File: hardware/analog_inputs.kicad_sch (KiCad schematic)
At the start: 0 parts

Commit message: Add the Cube project
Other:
- sheet Analog Input 1 ports: added REF; removed none
- sheet Analog Input 2 ports: added REF; removed none
- sheet Analog Input 3 ports: added REF; removed none
- sheet Analog Input 4 ports: added REF; removed none
- title: (none) -> Analog Inputs
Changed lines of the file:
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@@
   (paper "A4")
   (title_block
-    (date "2023-06-06")
+    (title "Analog Inputs")
+    (date "2023-07-01")
     (rev "${REVISION}")
     (company "Author: I. Kajdan")
     (comment 1 "Reviewer:")
   )
-  (wire (pts (xy 133.35 107.95) (xy 134.62 107.95))
+  (wire (pts (xy 135.89 104.14) (xy 137.16 104.14))
     (stroke (width 0) (type default))
   )
-  (wire (pts (xy 162.56 96.52) (xy 163.83 96.52))
+  (wire (pts (xy 165.1 92.71) (xy 166.37 92.71))
     (stroke (width 0) (type default))
   )
-  (wire (pts (xy 133.35 85.09) (xy 134.62 85.09))
+  (wire (pts (xy 135.89 107.95) (xy 137.16 107.95))
     (stroke (width 0) (type default))
   )
-  (wire (pts (xy 162.56 119.38) (xy 163.83 119.38))
+  (wire (pts (xy 135.89 81.28) (xy 137.16 81.28))
     (stroke (width 0) (type default))
   )
-  (wire (pts (xy 133.35 119.38) (xy 134.62 119.38))
+  (wire (pts (xy 165.1 115.57) (xy 166.37 115.57))
     (stroke (width 0) (type default))
   )
-  (wire (pts (xy 162.56 85.09) (xy 163.83 85.09))
+  (wire (pts (xy 135.89 115.57) (xy 137.16 115.57))
     (stroke (width 0) (type default))
   )
-  (wire (pts (xy 162.56 107.95) (xy 163.83 107.95))
+  (wire (pts (xy 135.89 96.52) (xy 137.16 96.52))
     (stroke (width 0) (type default))
   )
-  (wire (pts (xy 133.35 96.52) (xy 134.62 96.52))
+  (wire (pts (xy 135.89 119.38) (xy 137.16 119.38))
     (stroke (width 0) (type default))
   )
-  (hierarchical_label "IN4" (shape input) (at 133.35 119.38 180) (fields_autoplaced)
+  (wire (pts (xy 165.1 81.28) (xy 166.37 81.28))
+    (stroke (width 0) (type default))
+  )
+  (wire (pts (xy 135.89 85.09) (xy 137.16 85.09))
+    (stroke (width 0) (type default))
+  )
+  (wire (pts (xy 165.1 104.14) (xy 166.37 104.14))
+    (stroke (width 0) (type default))
+  )
+  (wire (pts (xy 135.89 92.71) (xy 137.16 92.71))
+    (stroke (width 0) (type default))
+  )
+  (hierarchical_label "REF1" (shape input) (at 135.89 107.95 180) (fields_autoplaced)
     (effects (font (size 1.27 1.27)) (justify right))
   )
-  (hierarchical_label "OUT2" (shape output) (at 163.83 96.52 0) (fields_autoplaced)
+  (hierarchical_label "IN4" (shape input) (at 135.89 115.57 180) (fields_autoplaced)
+    (effects (font (size 1.27 1.27)) (justify right))
+  )
+  (hierarchical_label "OUT2" (shape output) (at 166.37 92.71 0) (fields_autoplaced)
     (effects (font (size 1.27 1.27)) (justify left))
   )
-  (hierarchical_label "OUT4" (shape output) (at 163.83 119.38 0) (fields_autoplaced)
+  (hierarchical_label "REF2" (shape input) (at 135.89 96.52 180) (fields_autoplaced)
+    (effects (font (size 1.27 1.27)) (justify right))
+  )
+  (hierarchical_label "OUT4" (shape output) (at 166.37 115.57 0) (fields_autoplaced)
     (effects (font (size 1.27 1.27)) (justify left))
   )
-  (hierarchical_label "IN3" (shape input) (at 133.35 107.95 180) (fields_autoplaced)
+  (hierarchical_label "REF2" (shape input) (at 135.89 119.38 180) (fields_autoplaced)
     (effects (font (size 1.27 1.27)) (justify right))
   )
-  (hierarchical_label "OUT3" (shape output) (at 163.83 107.95 0) (fields_autoplaced)
+  (hierarchical_label "REF1" (shape input) (at 135.89 85.09 180) (fields_autoplaced)
+    (effects (font (size 1.27 1.27)) (justify right))
+  )
+  (hierarchical_label "IN3" (shape input) (at 135.89 104.14 180) (fields_autoplaced)
+    (effects (font (size 1.27 1.27)) (justify right))
+  )
+  (hierarchical_label "OUT3" (shape output) (at 166.37 104.14 0) (fields_autoplaced)
     (effects (font (size 1.27 1.27)) (justify left))
   )
-  (hierarchical_label "IN1" (shape input) (at 133.35 85.09 180) (fields_autoplaced)
+  (hierarchical_label "IN1" (shape input) (at 135.89 81.28 180) (fields_autoplaced)
     (effects (font (size 1.27 1.27)) (justify right))
   )
-  (hierarchical_label "OUT1" (shape output) (at 163.83 85.09 0) (fields_autoplaced)
+  (hierarchical_label "OUT1" (shape output) (at 166.37 81.28 0) (fields_autoplaced)
     (effects (font (size 1.27 1.27)) (justify left))
   )
-  (hierarchical_label "IN2" (shape input) (at 133.35 96.52 180) (fields_autoplaced)
+  (hierarchical_label "IN2" (shape input) (at 135.89 92.71 180) (fields_autoplaced)
     (effects (font (size 1.27 1.27)) (justify right))
   )
-  (sheet (at 134.62 81.28) (size 27.94 7.62)
+  (sheet (at 137.16 78.74) (size 27.94 8.89)
     (stroke (width 0.1524) (type solid))
     (fill (color 0 0 0 0.0000))
-    (property "Sheetname" "Analog Input 1" (at 148.59 84.3784 0)
-      (effects (font (size 1.27 1.27)) (justify top))
+    (property "Sheetname" "Analog Input 1" (at 151.13 83.1084 0)
+      (effects (font (size 1.27 1.27)))
     )
-    (property "Sheetfile" "analog_input.kicad_sch" (at 134.62 98.3746 0)
+    (property "Sheetfile" "analog_input.kicad_sch" (at 137.16 95.8346 0)
       (effects (font (size 1.27 1.27)) (justify left top) hide)
     )
-    (pin "IN" input (at 134.62 85.09 180)
+    (pin "IN" input (at 137.16 81.28 180)
       (effects (font (size 1.27 1.27)) (justify left))
     )
-    (pin "OUT" output (at 162.56 85.09 0)
+    (pin "OUT" output (at 165.1 81.28 0)
       (effects (font (size 1.27 1.27)) (justify right))
+    )
+    (pin "REF" input (at 137.16 85.09 180)
+      (effects (font (size 1.27 1.27)) (justify left))
     )
     (instances
@@
     )
   )
-  (sheet (at 134.62 104.14) (size 27.94 7.62)
+  (sheet (at 137.16 101.6) (size 27.94 8.89)
     (stroke (width 0.1524) (type solid))
     (fill (color 0 0 0 0.0000))
-    (property "Sheetname" "Analog Input 3" (at 148.59 107.2384 0)
+    (property "Sheetname" "Analog Input 3" (at 151.13 104.6984 0)
       (effects (font (size 1.27 1.27)) (justify top))
     )
-    (property "Sheetfile" "analog_input.kicad_sch" (at 134.62 121.2346 0)
+    (property "Sheetfile" "analog_input.kicad_sch" (at 137.16 118.6946 0)
       (effects (font (size 1.27 1.27)) (justify left top) hide)
     )
-    (pin "IN" input (at 134.62 107.95 180)
+    (pin "IN" input (at 137.16 104.14 180)
       (effects (font (size 1.27 1.27)) (justify left))
     )
-    (pin "OUT" output (at 162.56 107.95 0)
+    (pin "OUT" output (at 165.1 104.14 0)
       (effects (font (size 1.27 1.27)) (justify right))
+    )
+    (pin "REF" input (at 137.16 107.95 180)
+      (effects (font (size 1.27 1.27)) (justify left))
     )
     (instances
@@
     )
   )
-  (sheet (at 134.62 115.57) (size 27.94 7.62)
+  (sheet (at 137.16 113.03) (size 27.94 8.89)
     (stroke (width 0.1524) (type solid))
     (fill (color 0 0 0 0.0000))
-    (property "Sheetname" "Analog Input 4" (at 148.59 118.6684 0)
+    (property "Sheetname" "Analog Input 4" (at 151.13 116.1284 0)
       (effects (font (size 1.27 1.27)) (justify top))
     )
-    (property "Sheetfile" "analog_input.kicad_sch" (at 134.62 132.6646 0)
+    (property "Sheetfile" "analog_input.kicad_sch" (at 137.16 130.1246 0)
       (effects (font (size 1.27 1.27)) (justify left top) hide)
     )
-    (pin "IN" input (at 134.62 119.38 180)
+    (pin "IN" input (at 137.16 115.57 180)
       (effects (font (size 1.27 1.27)) (justify left))
     )
-    (pin "OUT" output (at 162.56 119.38 0)
+    (pin "OUT" output (at 165.1 115.57 0)
       (effects (font (size 1.27 1.27)) (justify right))
+    )
+    (pin "REF" input (at 137.16 119.38 180)
+      (effects (font (size 1.27 1.27)) (justify left))
     )
     (instances
@@
     )
   )
-  (sheet (at 134.62 92.71) (size 27.94 7.62)
+  (sheet (at 137.16 90.17) (size 27.94 8.89)
     (stroke (width 0.1524) (type solid))
     (fill (color 0 0 0 0.0000))
-    (property "Sheetname" "Analog Input 2" (at 148.59 95.8084 0)
+    (property "Sheetname" "Analog Input 2" (at 151.13 93.2684 0)
       (effects (font (size 1.27 1.27)) (justify top))
     )
-    (property "Sheetfile" "analog_input.kicad_sch" (at 134.62 109.8046 0)
+    (property "Sheetfile" "analog_input.kicad_sch" (at 137.16 107.2646 0)
       (effects (font (size 1.27 1.27)) (justify left top) hide)
     )
-    (pin "IN" input (at 134.62 96.52 180)
+    (pin "IN" input (at 137.16 92.71 180)
       (effects (font (size 1.27 1.27)) (justify left))
     )
-    (pin "OUT" output (at 162.56 96.52 0)
+    (pin "OUT" output (at 165.1 92.71 0)
       (effects (font (size 1.27 1.27)) (justify right))
     )
+    (pin "REF" input (at 137.16 96.52 180)
+      (effects (font (size 1.27 1.27)) (justify left))
+    )
     (instances

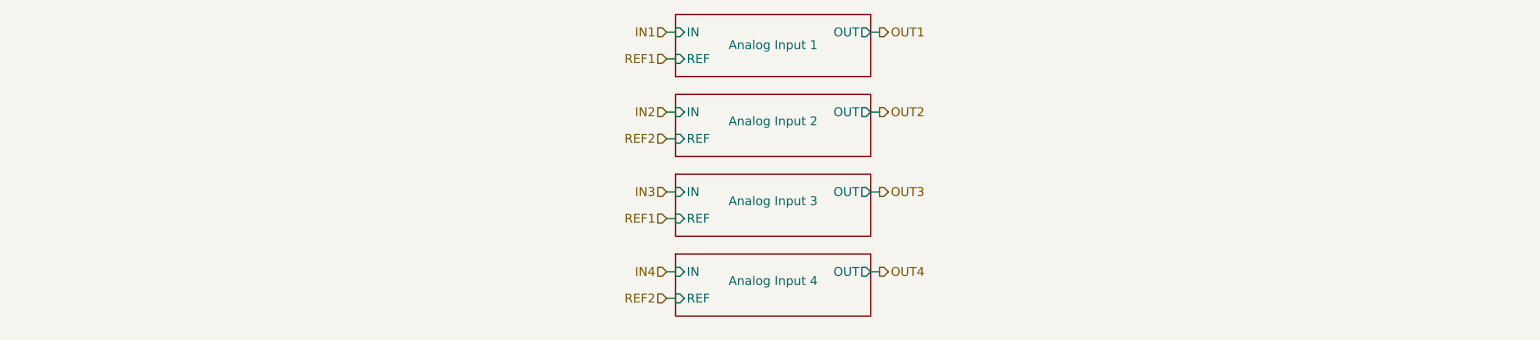
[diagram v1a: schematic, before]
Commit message: Improve the schematic
- add anti-aliasing filters
- rearrange the main connector signals
- improve the power filtering
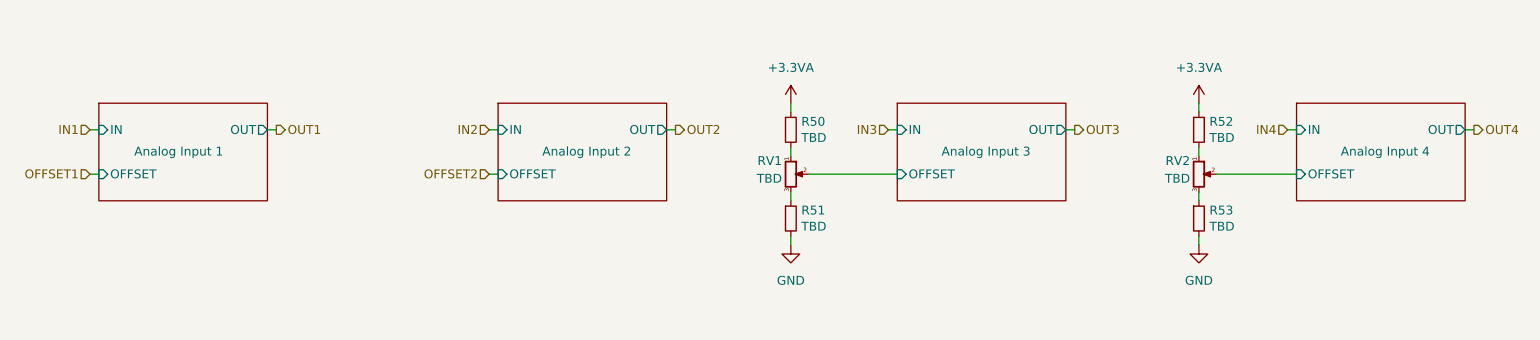
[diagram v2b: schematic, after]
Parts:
- added R50, R51, R52, R53: TBD, Resistor_SMD:R_0603_1608Metric_Pad0.98x0.95mm_HandSolder, symbol Device:R_Small
- added RV1, RV2: TBD, Potentiometer_SMD:Potentiometer_Bourns_3214J_Horizontal, symbol Device:R_Potentiometer_Small
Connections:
- new net: R51.1, RV1.3
- new net: R52.2, RV2.1
- new net: R50.2, RV1.1
- new net: R53.1, RV2.3
- new net +3.3VA: R50.1, R52.1
- new net Analog Input 3/OFFSET: RV1.2
- new net Analog Input 4/OFFSET: RV2.2
- new net GND: R51.2, R53.2
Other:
- sheet Analog Input 1 ports: added OFFSET; removed REF
- sheet Analog Input 2 ports: added OFFSET; removed REF
- sheet Analog Input 3 ports: added OFFSET; removed REF
- sheet Analog Input 4 ports: added OFFSET; removed REF

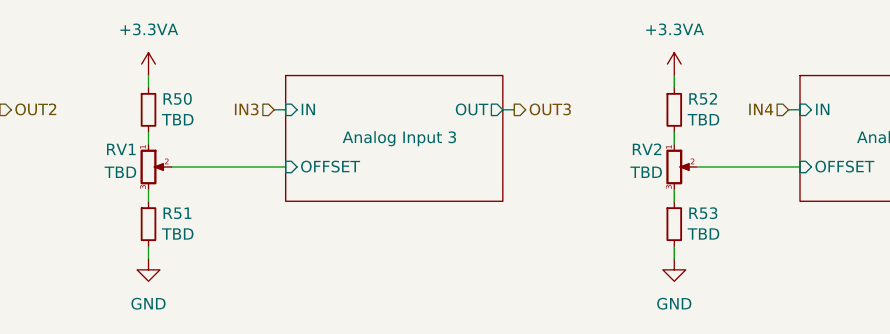
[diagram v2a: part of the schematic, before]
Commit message: Set component values
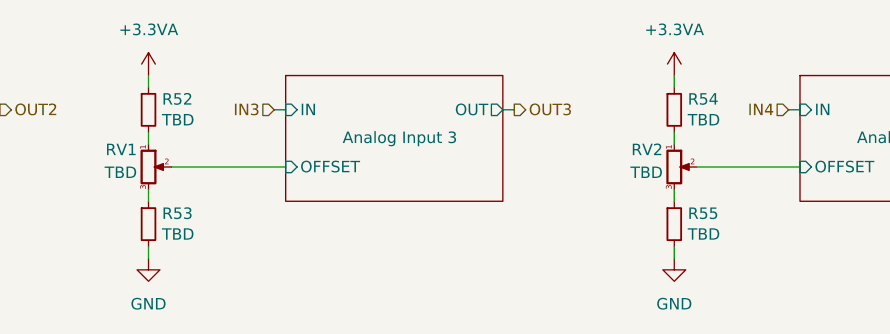
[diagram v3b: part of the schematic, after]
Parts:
- R52: renamed from R50; footprint Resistor_SMD:R_0603_1608Metric_Pad0.98x0.95mm_HandSolder -> Resistor_SMD:R_0603_1608Metric
- R53: renamed from R51; footprint Resistor_SMD:R_0603_1608Metric_Pad0.98x0.95mm_HandSolder -> Resistor_SMD:R_0603_1608Metric
- R54: renamed from R52; footprint Resistor_SMD:R_0603_1608Metric_Pad0.98x0.95mm_HandSolder -> Resistor_SMD:R_0603_1608Metric
- R55: renamed from R53; footprint Resistor_SMD:R_0603_1608Metric_Pad0.98x0.95mm_HandSolder -> Resistor_SMD:R_0603_1608Metric
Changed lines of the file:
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@@
   (symbol (lib_id "Device:R_Small") (at 153.67 107.95 0) (unit 1)
     (in_bom yes) (on_board yes) (dnp no)
-    (property "Reference" "R51" (at 155.1686 106.7816 0)
+    (property "Reference" "R53" (at 155.1686 106.7816 0)
       (effects (font (size 1.27 1.27)) (justify left))
     )
@@
       (effects (font (size 1.27 1.27)) (justify left))
     )
-    (property "Footprint" "Resistor_SMD:R_0603_1608Metric_Pad0.98x0.95mm_HandSolder" (at 153.67 107.95 0)
+    (property "Footprint" "Resistor_SMD:R_0603_1608Metric" (at 153.67 107.95 0)
       (effects (font (size 1.27 1.27)) hide)
     )
@@
       (project "rearbox"
         (path "/b652b05a-4e3d-4ad1-b032-18886abe7d45/264ec557-c33b-4d6e-8249-7c546f6f500a"
-          (reference "R51") (unit 1)
+          (reference "R53") (unit 1)
         )
       )
@@
   (symbol (lib_id "Device:R_Small") (at 212.09 95.25 0) (unit 1)
     (in_bom yes) (on_board yes) (dnp no)
-    (property "Reference" "R52" (at 213.5886 94.0816 0)
+    (property "Reference" "R54" (at 213.5886 94.0816 0)
       (effects (font (size 1.27 1.27)) (justify left))
     )
@@
       (effects (font (size 1.27 1.27)) (justify left))
     )
-    (property "Footprint" "Resistor_SMD:R_0603_1608Metric_Pad0.98x0.95mm_HandSolder" (at 212.09 95.25 0)
+    (property "Footprint" "Resistor_SMD:R_0603_1608Metric" (at 212.09 95.25 0)
       (effects (font (size 1.27 1.27)) hide)
     )
     (property "Datasheet" "~" (at 212.09 95.25 0)
+      (effects (font (size 1.27 1.27)) hide)
+    )
+    (pin "1")
+    (pin "2")
+    (instances
+      (project "rearbox"
+        (path "/b652b05a-4e3d-4ad1-b032-18886abe7d45/264ec557-c33b-4d6e-8249-7c546f6f500a"
+          (reference "R54") (unit 1)
+        )
+      )
+      (project "apps"
+        (path "/fc4ad874-c922-4070-89f9-7262080469d8/00000000-0000-0000-0000-00006068dc5c"
+          (reference "R7") (unit 1)
+        )
+      )
+    )
+  )
+  (symbol (lib_id "Device:R_Small") (at 153.67 95.25 0) (unit 1)
+    (in_bom yes) (on_board yes) (dnp no)
+    (property "Reference" "R52" (at 155.1686 94.0816 0)
+      (effects (font (size 1.27 1.27)) (justify left))
+    )
+    (property "Value" "TBD" (at 155.1686 96.393 0)
+      (effects (font (size 1.27 1.27)) (justify left))
+    )
+    (property "Footprint" "Resistor_SMD:R_0603_1608Metric" (at 153.67 95.25 0)
+      (effects (font (size 1.27 1.27)) hide)
+    )
+    (property "Datasheet" "~" (at 153.67 95.25 0)
       (effects (font (size 1.27 1.27)) hide)
     )
@@
     )
   )
-  (symbol (lib_id "Device:R_Small") (at 153.67 95.25 0) (unit 1)
-    (in_bom yes) (on_board yes) (dnp no)
-    (property "Reference" "R50" (at 155.1686 94.0816 0)
-      (effects (font (size 1.27 1.27)) (justify left))
-    )
-    (property "Value" "TBD" (at 155.1686 96.393 0)
-      (effects (font (size 1.27 1.27)) (justify left))
-    )
-    (property "Footprint" "Resistor_SMD:R_0603_1608Metric_Pad0.98x0.95mm_HandSolder" (at 153.67 95.25 0)
-      (effects (font (size 1.27 1.27)) hide)
-    )
-    (property "Datasheet" "~" (at 153.67 95.25 0)
-      (effects (font (size 1.27 1.27)) hide)
-    )
-    (pin "1")
-    (pin "2")
-    (instances
-      (project "rearbox"
-        (path "/b652b05a-4e3d-4ad1-b032-18886abe7d45/264ec557-c33b-4d6e-8249-7c546f6f500a"
-          (reference "R50") (unit 1)
-        )
-      )
-      (project "apps"
-        (path "/fc4ad874-c922-4070-89f9-7262080469d8/00000000-0000-0000-0000-00006068dc5c"
-          (reference "R7") (unit 1)
-        )
-      )
-    )
-  )
   (symbol (lib_id "Device:R_Small") (at 212.09 107.95 0) (unit 1)
     (in_bom yes) (on_board yes) (dnp no)
-    (property "Reference" "R53" (at 213.5886 106.7816 0)
+    (property "Reference" "R55" (at 213.5886 106.7816 0)
       (effects (font (size 1.27 1.27)) (justify left))
     )
@@
       (effects (font (size 1.27 1.27)) (justify left))
     )
-    (property "Footprint" "Resistor_SMD:R_0603_1608Metric_Pad0.98x0.95mm_HandSolder" (at 212.09 107.95 0)
+    (property "Footprint" "Resistor_SMD:R_0603_1608Metric" (at 212.09 107.95 0)
       (effects (font (size 1.27 1.27)) hide)
     )
@@
       (project "rearbox"
         (path "/b652b05a-4e3d-4ad1-b032-18886abe7d45/264ec557-c33b-4d6e-8249-7c546f6f500a"
-          (reference "R53") (unit 1)
+          (reference "R55") (unit 1)
         )
       )
